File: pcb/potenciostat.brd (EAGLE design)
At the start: 65.7 x 56.1 mm, 30 parts, among them K2 ZNS5406, Q1 2N3904

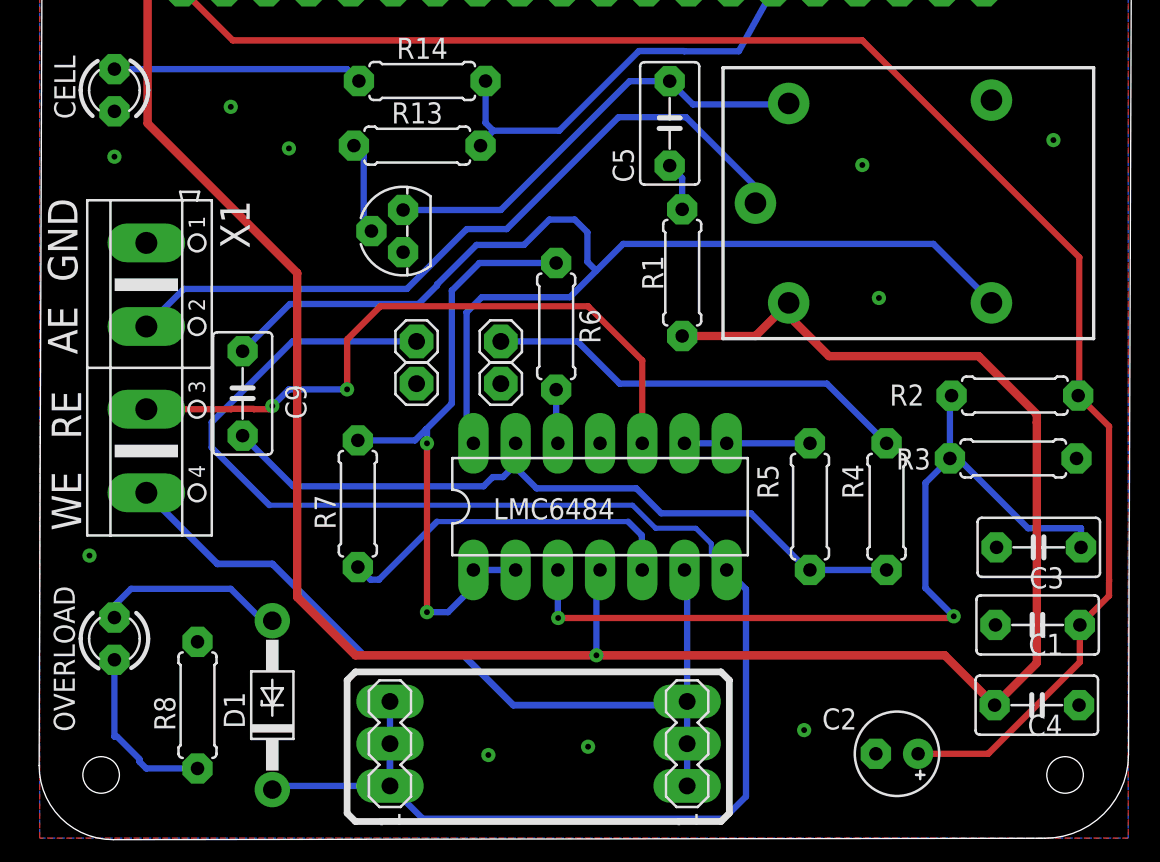
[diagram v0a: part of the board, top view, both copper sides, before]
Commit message: Remove prints and add docstrings
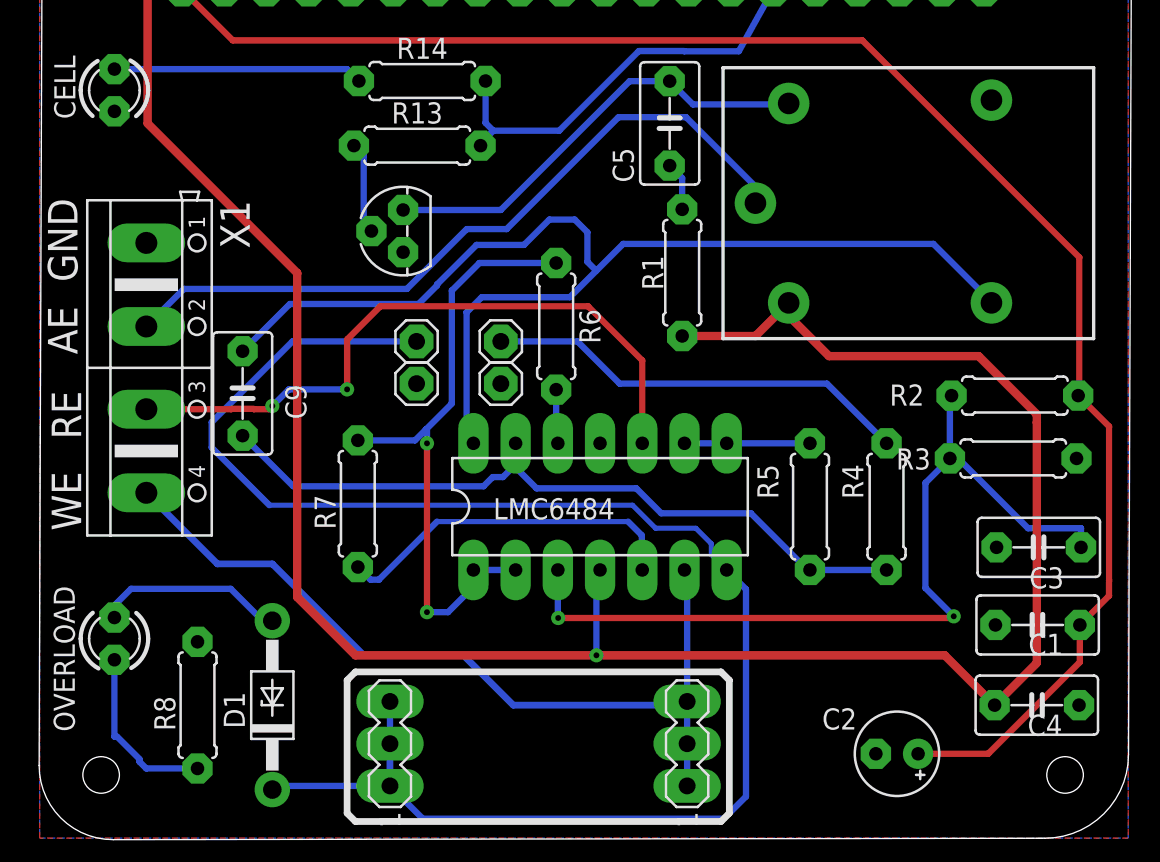
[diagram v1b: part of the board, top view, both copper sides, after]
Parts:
- R8: value 10K -> 1k
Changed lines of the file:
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@@
 <attribute name="OC_FARNELL" value="1612435" x="-61" y="12" size="1.778" layer="27" rot="R90" display="off"/>
 </element>
-<element name="R8" library="rcl" library_urn="urn:adsk.eagle:library:334" package="0207/7" package3d_urn="urn:adsk.eagle:package:23493/1" value="10K" x="-56" y="8" smashed="yes" rot="R270">
+<element name="R8" library="rcl" library_urn="urn:adsk.eagle:library:334" package="0207/7" package3d_urn="urn:adsk.eagle:package:23493/1" value="1k" x="-56" y="8" smashed="yes" rot="R270">
 <attribute name="NAME" x="-58.603" y="8.54" size="1.27" layer="25" ratio="10" rot="R270"/>
 <attribute name="SPICEPREFIX" value="R" x="-56" y="8" size="1.778" layer="27" rot="R270" display="off"/>
@@
 <wire x1="-61" y1="14" x2="-61" y2="13.27" width="0.381" layer="16"/>
 </signal>
-<signal name="N$7">
-<via x="-16" y="40.5" extent="1-16" drill="0.35"/>
-</signal>
-<signal name="N$9">
-<via x="-15" y="32.5" extent="1-16" drill="0.35"/>
-</signal>
-<signal name="N$11">
-<via x="-50.5" y="41.5" extent="1-16" drill="0.35"/>
-</signal>
-<signal name="N$12">
-<via x="-19.5" y="6.5" extent="1-16" drill="0.35"/>
-</signal>
-<signal name="N$13">
-<via x="-38.5" y="5" extent="1-16" drill="0.35"/>
-</signal>
-<signal name="N$14">
-<via x="-62.5" y="17" extent="1-16" drill="0.35"/>
-</signal>
-<signal name="N$17">
-<via x="-61" y="41" extent="1-16" drill="0.35"/>
-</signal>
-<signal name="N$19">
-<via x="-4.5" y="42" extent="1-16" drill="0.35"/>
-</signal>
-<signal name="N$20">
-<via x="-32.5" y="5.5" extent="1-16" drill="0.35"/>
-</signal>
-<signal name="N$21">
-<via x="-54" y="44" extent="1-16" drill="0.35"/>
-</signal>
 </signals>

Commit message: Corrigi pad do ad
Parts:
- moved JP2 65.0 mm to (27.2, 31.6)
- moved JP3 65.0 mm to (22.2, 29.0)
- moved JP4 65.0 mm to (22.2, 31.6)
- moved JP5 65.0 mm to (27.2, 29.0)
- moved C1 65.0 mm to (59.5, 13.3)
- moved C2 65.0 mm to (51.1, 5.57)
- moved C3 65.0 mm to (59.6, 18.0)
- moved C4 65.0 mm to (59.5, 8.50)
- moved C5 65.0 mm to (37.4, 43.5)
- moved C9 65.0 mm to (11.7, 27.3)
- moved CELL 65.0 mm to (4.00, 45.5)
- moved D1 65.0 mm to (13.5, 8.50)
- moved JP1 65.0 mm to (32.2, 57.9)
- moved K2 65.0 mm to (51.5, 38.7)
- moved LMC6484 65.0 mm to (33.2, 20.4)
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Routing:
- net N$18: track 5.58 -> 4.81 mm
- net REFEL: track 40.5 -> 41.2 mm
- net DA: track 25.7 -> 26.3 mm
- net AUX: track 69.8 -> 70.3 mm

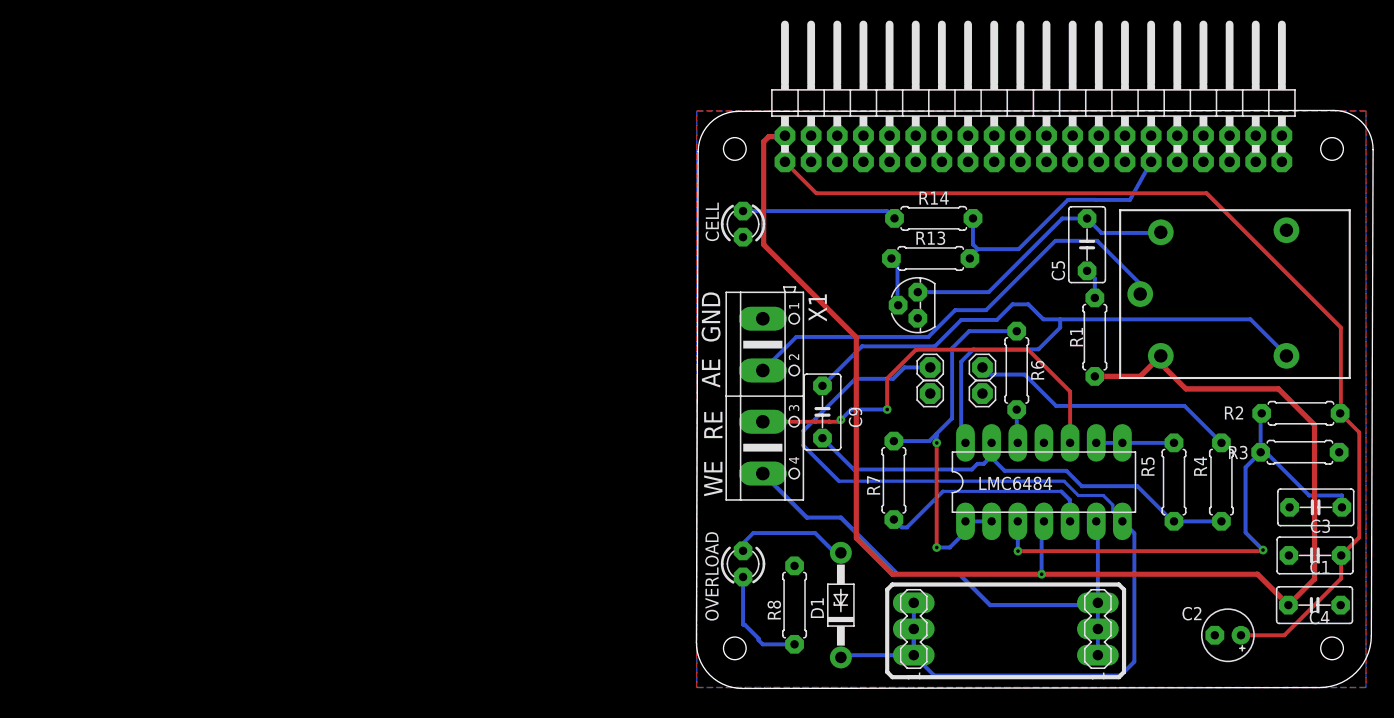
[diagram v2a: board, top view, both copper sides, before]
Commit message: Placa com seleção ganho
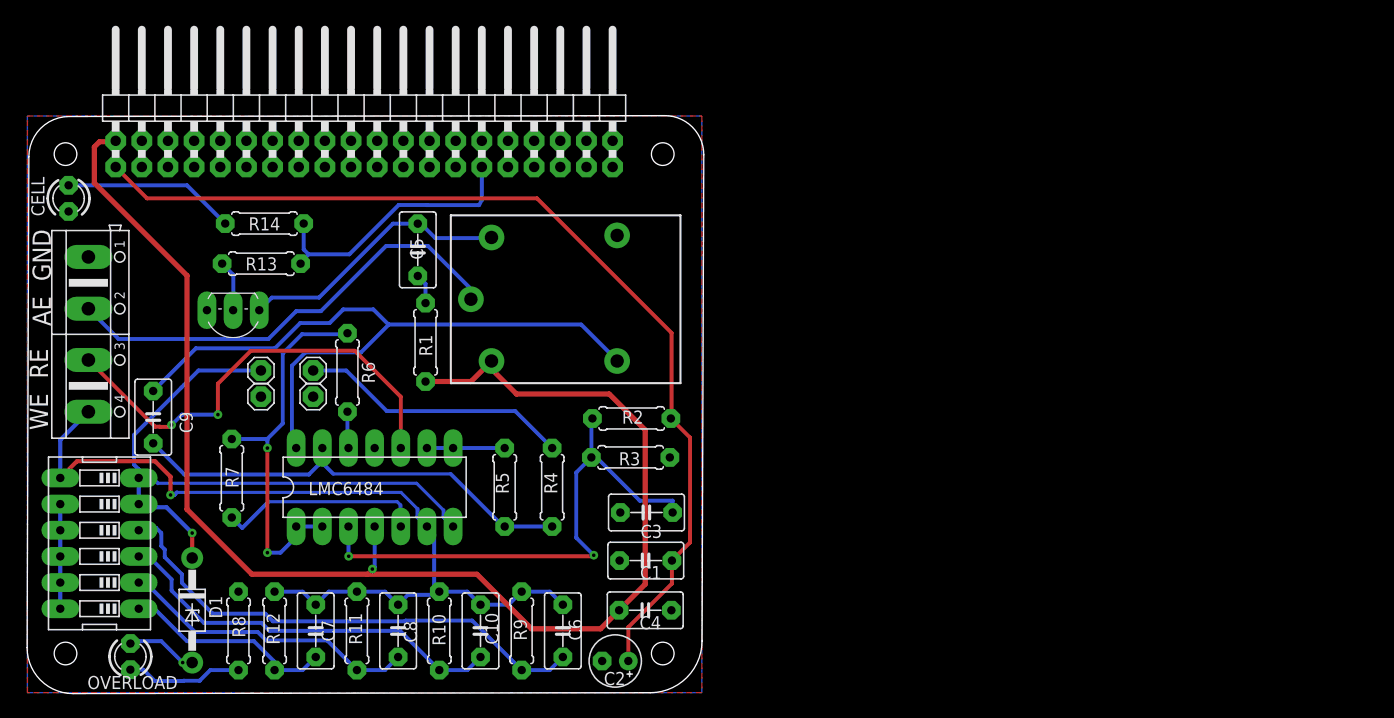
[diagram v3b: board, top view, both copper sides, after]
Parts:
- removed SV1, SV2: (no value), con-lstb:MA03-1
- added C10, C6, C7, C8: 1uF, rcl:C050-035X075
- added R10: 47K, rcl:0207/7
- added R11: 4K7, rcl:0207/7
- added R12: 470, rcl:0207/7
- added R9: 470K, rcl:0207/7
- added SW1: (no value), special:EDG-06
- Q1: value 2N3904 -> BC548; device transistor-small-signal:TO92D -> transistor-npn:TO92-EBC
- moved Q1 66.5 mm to (-45.5, 35.9), turned to 180 degrees
- moved X1 65.8 mm to (-59.6, 34.8)
- moved CELL 65.5 mm to (-61.5, 48.0)
- moved C1 65.0 mm to (-5.45, 12.8)
- moved C3 65.0 mm to (-5.38, 17.5)
- moved C4 65.0 mm to (-5.50, 8.00)
- moved C5 65.0 mm to (-27.6, 43.0)
- moved C9 65.0 mm to (-53.3, 26.8)
- moved JP1 65.0 mm to (-32.8, 57.4)
- moved K2 65.0 mm to (-13.5, 38.2)
- moved LMC6484 65.0 mm to (-31.8, 19.9)
- moved R1 65.0 mm to (-26.8, 34.0)
- moved R13 65.0 mm to (-42.8, 41.7)
- moved R14 65.0 mm to (-42.5, 45.6)
- moved R2 65.0 mm to (-6.82, 26.6)
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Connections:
- new net N$11: C8.2, R11.1, SW1.2
- new net N$12: C10.2, R10.1, SW1.3
- new net N$13: C6.2, R9.1, SW1.4
- new net N$7: C7.2, R12.1, SW1.1
- new net N$9: SW1.10, SW1.11, SW1.12, SW1.8, SW1.9
- net AD: now also SW1.5, SW1.6; no longer SV1.1, SV1.2, SV1.3
- net WEL: now also C10.1, C6.1, C7.1, C8.1, R10.2, R11.2, R12.2, R9.2, SW1.7; no longer SV2.1, SV2.2, SV2.3
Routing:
- net N$13: track 0.00 -> 49.3 mm
- net AD: track 102.6 -> 63.5 mm, vias 0 -> 1
- net N$12: track 0.00 -> 38.9 mm
- net WEL: track 51.2 -> 87.2 mm, vias 0 -> 1
- net N$11: track 0.00 -> 29.5 mm
- net N$7: track 0.00 -> 20.7 mm
- net N$9: track 0.00 -> 10.2 mm
- net N$10: track 11.4 -> 6.96 mm, vias 0 -> 1
- net REFEL: track 41.2 -> 44.7 mm
- net 3V3: track 98.6 -> 95.8 mm
- net N$16: track 15.8 -> 17.5 mm
- net GPIO: track 25.4 -> 26.7 mm
- net N$8: track 21.3 -> 20.1 mm
- net N$1: track 10.5 -> 11.4 mm
- net VCC/2: track 39.0 -> 38.2 mm
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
